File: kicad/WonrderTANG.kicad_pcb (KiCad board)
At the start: 2 copper layers, 99.9 x 89.5 mm, 28 parts, among them CON1 MSX-CONNECTOR, J2 AudioJack3, J3 AUDIO, Q1 2N3904, Q2 2N3904, U1 SN74LVC245AN, U2 SN74LVC245AN, U3 SN74LVC245AN, U4 SN74LVC245AN, U5 Tang_Nano_20k, U6 SN74LVC245AN

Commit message: silk update
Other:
- board text added: "2024 V2.0b (RCC REV 0) LUIS ANTONIOSI"
- board text removed: "2024 V2.0b LUIS ANTONIOSI"
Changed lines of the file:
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@@
 		(title "MSX-IDE 2021")
 		(date "2021-08-05")
-		(rev "2.0b _rcc_0")
+		(rev "2.0b (RCC Rev 0)")
 		(company "MSXmakers")
 		(comment 1 "Original board design, but sizes reduced and removed solder mask in the edge connenctor.")
@@
 		)
 	)
-	(gr_text "2024 V2.0b\nLUIS ANTONIOSI"
+	(gr_text "2024 V2.0b (RCC REV 0)\nLUIS ANTONIOSI"
 		(at 82.225 105.41 90)
 		(layer "F.SilkS")

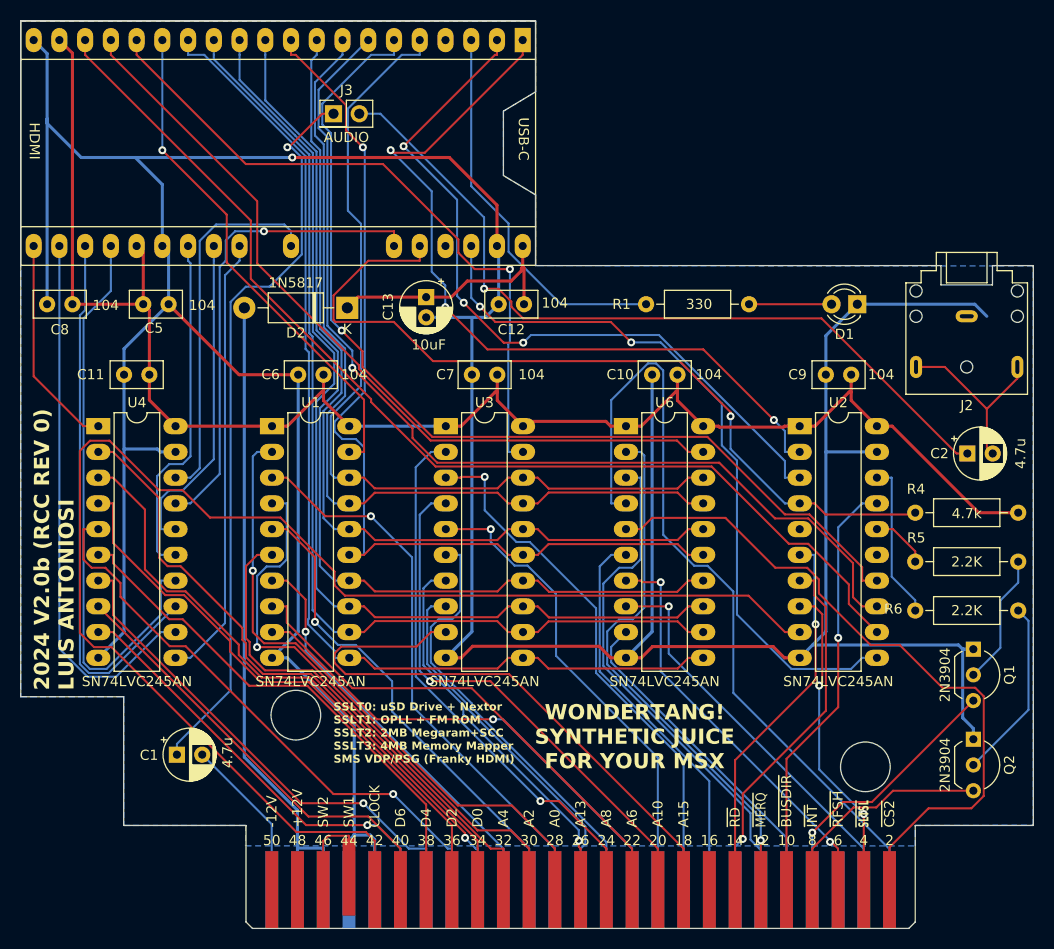
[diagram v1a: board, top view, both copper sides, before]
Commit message: Version 2.0b RCC Rev1 - rotated J3 to better fit audio jumper
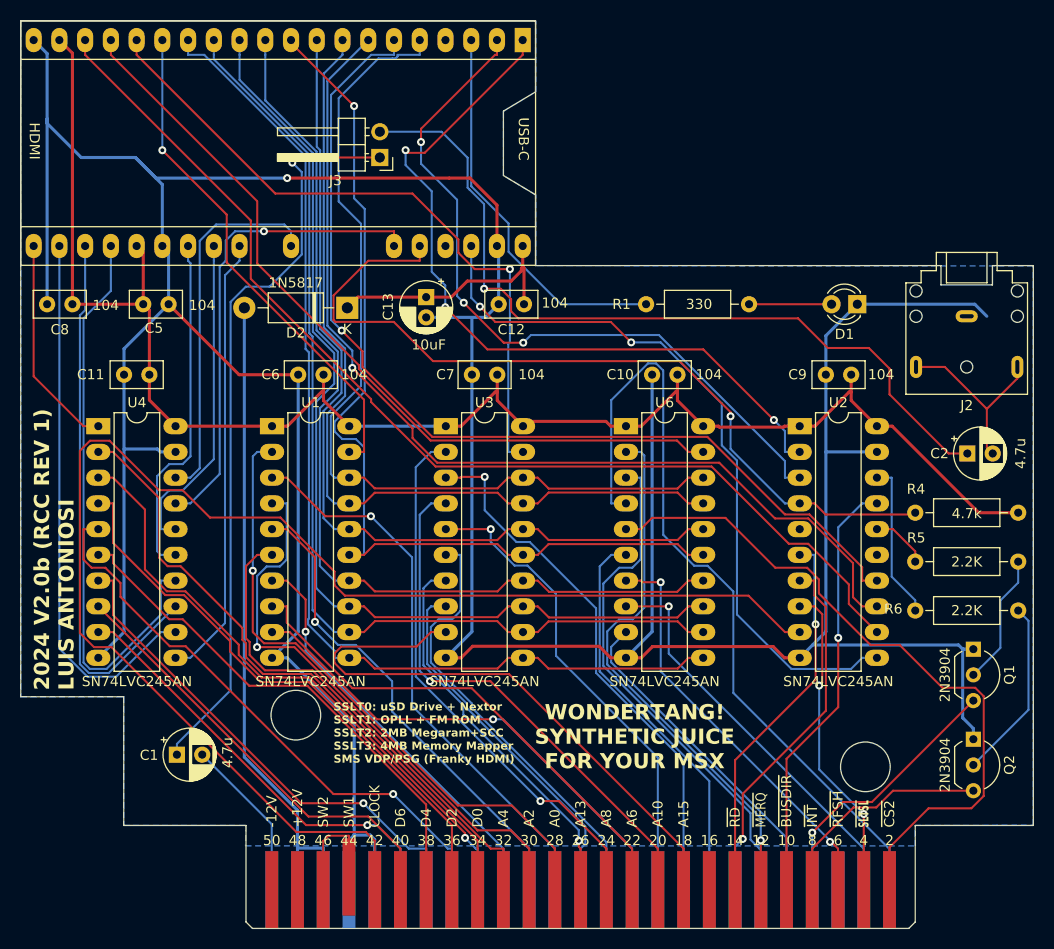
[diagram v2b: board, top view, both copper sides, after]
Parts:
- D1: value uSD -> LED
- J3: value AUDIO -> Conn_02x01; footprint Connector_PinHeader_2.54mm:PinHeader_2x01_P2.54mm_Vertical -> Connector_PinHeader_2.54mm:PinHeader_1x02_P2.54mm_Horizontal
- moved J3 6.29 mm to (112.3, 52.8), turned to 180 degrees
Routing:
- net INT_33: track 78.4 -> 76.3 mm
- net MP0_33: track 87.2 -> 89.2 mm
- net Net-(J3-Pin_2): track 78.3 -> 79.9 mm
- net BUSDIR_33: track 74.2 -> 72.8 mm
- net Net-(J3-Pin_1): track 73.2 -> 74.1 mm
- net WR_33: track 99.8 -> 99.1 mm
- net MP1_33: track 87.3 -> 86.5 mm
- net RD_33: track 98.4 -> 97.7 mm
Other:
- board text added: "2024 V2.0b (RCC REV 1) LUIS ANTONIOSI"
- board text removed: "2024 V2.0b (RCC REV 0) LUIS ANTONIOSI"
